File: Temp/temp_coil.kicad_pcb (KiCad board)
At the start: 2 copper layers, 0 parts

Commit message: Updated GUI
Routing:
- net (no net): track 60.0 -> 1086.3 mm

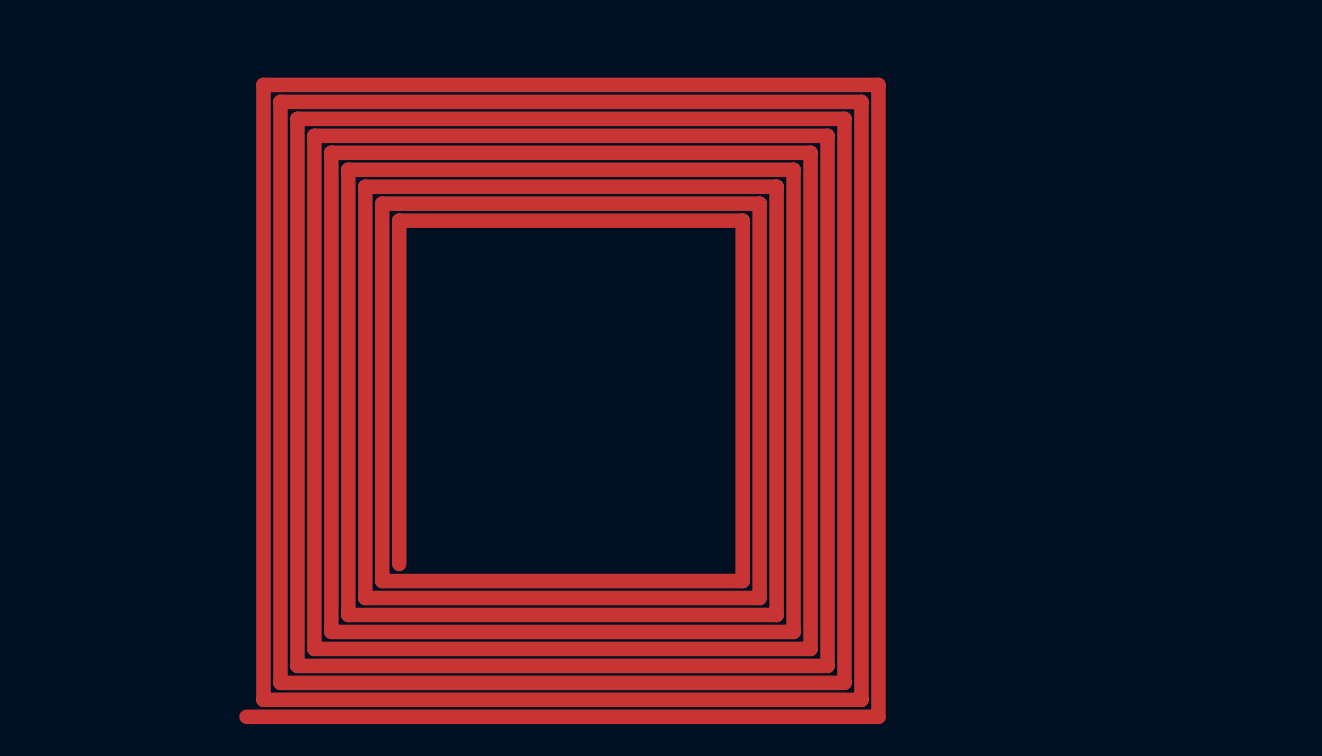
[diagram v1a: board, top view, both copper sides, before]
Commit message: Better Square coil calculation
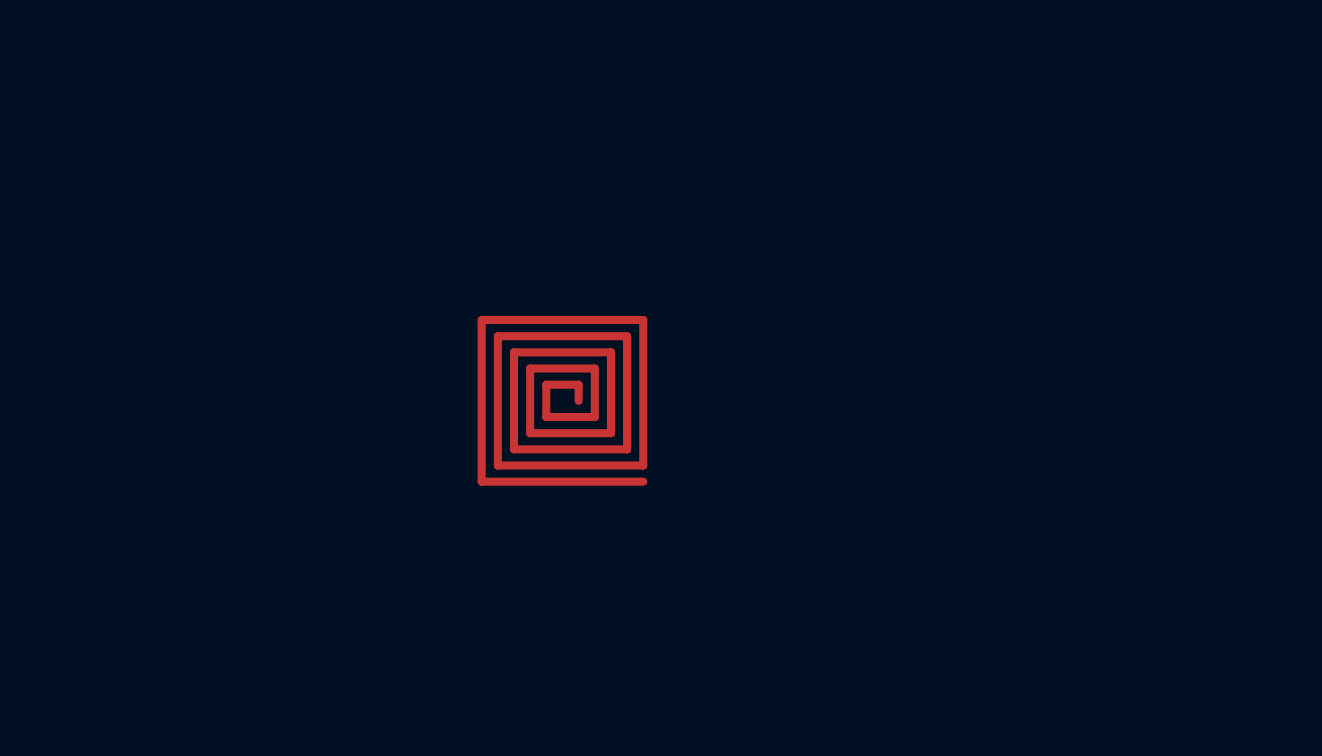
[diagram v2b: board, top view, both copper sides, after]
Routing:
- net (no net): track 1086.3 -> 119.0 mm
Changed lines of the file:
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@@
 	(net 0 "")
 	(segment
-		(start 165.35 84.65)
-		(end 135.7 84.65)
-		(width 0.9)
+		(start 151 99)
+		(end 151 100)
+		(width 0.5)
 		(layer "F.Cu")
 		(net 0)
 	)
 	(segment
-		(start 130.449999 119.55)
-		(end 169.55 119.55)
-		(width 0.9)
+		(start 153 97)
+		(end 153 102)
+		(width 0.5)
 		(layer "F.Cu")
 		(net 0)
 	)
 	(segment
-		(start 131.5 80.45)
-		(end 131.5 118.5)
-		(width 0.9)
+		(start 154 96)
+		(end 154 103)
+		(width 0.5)
 		(layer "F.Cu")
 		(net 0)
 	)
 	(segment
-		(start 162.2 112.2)
-		(end 162.2 87.8)
-		(width 0.9)
+		(start 153 102)
+		(end 148 102)
+		(width 0.5)
 		(layer "F.Cu")
 		(net 0)
 	)
 	(segment
-		(start 136.75 113.25)
-		(end 163.25 113.25)
-		(width 0.9)
+		(start 147 103)
+		(end 147 97)
+		(width 0.5)
 		(layer "F.Cu")
 		(net 0)
 	)
 	(segment
-		(start 138.85 111.15)
-		(end 161.15 111.15)
-		(width 0.9)
+		(start 148 102)
+		(end 148 98)
+		(width 0.5)
 		(layer "F.Cu")
 		(net 0)
 	)
 	(segment
-		(start 137.8 112.2)
-		(end 162.2 112.2)
-		(width 0.9)
+		(start 147 97)
+		(end 153 97)
+		(width 0.5)
 		(layer "F.Cu")
 		(net 0)
 	)
 	(segment
-		(start 168.5 118.5)
-		(end 168.5 81.5)
-		(width 0.9)
+		(start 149 101)
+		(end 149 99)
+		(width 0.5)
 		(layer "F.Cu")
 		(net 0)
 	)
 	(segment
-		(start 163.25 113.25)
-		(end 163.25 86.75)
-		(width 0.9)
+		(start 146 104)
+		(end 146 96)
+		(width 0.5)
 		(layer "F.Cu")
 		(net 0)
 	)
 	(segment
-		(start 165.35 115.35)
-		(end 165.35 84.65)
-		(width 0.9)
+		(start 149 99)
+		(end 151 99)
+		(width 0.5)
 		(layer "F.Cu")
 		(net 0)
 	)
 	(segment
-		(start 164.3 85.7)
-		(end 136.75 85.7)
-		(width 0.9)
+		(start 145 105)
+		(end 145 95)
+		(width 0.5)
 		(layer "F.Cu")
 		(net 0)
 	)
 	(segment
-		(start 166.4 116.4)
-		(end 166.4 83.6)
-		(width 0.9)
+		(start 152 101)
+		(end 149 101)
+		(width 0.5)
 		(layer "F.Cu")
 		(net 0)
 	)
 	(segment
-		(start 137.8 86.75)
-		(end 137.8 112.2)
-		(width 0.9)
+		(start 152 98)
+		(end 152 101)
+		(width 0.5)
 		(layer "F.Cu")
 		(net 0)
 	)
 	(segment
-		(start 132.55 117.45)
-		(end 167.45 117.45)
-		(width 0.9)
+		(start 155 105)
+		(end 145 105)
+		(width 0.5)
 		(layer "F.Cu")
 		(net 0)
 	)
 	(segment
-		(start 167.45 82.55)
-		(end 133.6 82.55)
-		(width 0.9)
+		(start 146 96)
+		(end 154 96)
+		(width 0.5)
 		(layer "F.Cu")
 		(net 0)
 	)
 	(segment
-		(start 135.7 84.65)
-		(end 135.7 114.3)
-		(width 0.9)
+		(start 155 104)
+		(end 146 104)
+		(width 0.5)
 		(layer "F.Cu")
 		(net 0)
 	)
 	(segment
-		(start 161.15 88.85)
-		(end 139.9 88.85)
-		(width 0.9)
+		(start 148 98)
+		(end 152 98)
+		(width 0.5)
 		(layer "F.Cu")
 		(net 0)
 	)
 	(segment
-		(start 163.25 86.75)
-		(end 137.8 86.75)
-		(width 0.9)
+		(start 145 95)
+		(end 155 95)
+		(width 0.5)
 		(layer "F.Cu")
 		(net 0)
 	)
 	(segment
-		(start 135.7 114.3)
-		(end 164.3 114.3)
-		(width 0.9)
+		(start 154 103)
+		(end 147 103)
+		(width 0.5)
 		(layer "F.Cu")
 		(net 0)
 	)
 	(segment
-		(start 136.75 85.7)
-		(end 136.75 113.25)
-		(width 0.9)
+		(start 155 95)
+		(end 155 104)
+		(width 0.5)
 		(layer "F.Cu")
 		(net 0)
-	)
-	(segment
-		(start 134.65 83.6)
-		(end 134.65 115.35)
-		(width 0.9)
-		(layer "F.Cu")
-		(net 0)
-	)
-	(segment
-		(start 133.6 116.4)
-		(end 166.4 116.4)
-		(width 0.9)
-		(layer "F.Cu")
-		(net 0)
-	)
-	(segment
-		(start 167.45 117.45)
-		(end 167.45 82.55)
-		(width 0.9)
-		(layer "F.Cu")
-		(net 0)
-	)
-	(segment
-		(start 133.6 82.55)
-		(end 133.6 116.4)
-		(width 0.9)
-		(layer "F.Cu")
-		(net 0)
-	)
-	(segment
-		(start 134.65 115.35)
-		(end 165.35 115.35)
-		(width 0.9)
-		(layer "F.Cu")
-		(net 0)
-	)
-	(segment
-		(start 132.55 81.5)
-		(end 132.55 117.45)
-		(width 0.9)
-		(layer "F.Cu")
-		(net 0)
-	)
-	(segment
-		(start 164.3 114.3)
-		(end 164.3 85.7)
-		(width 0.9)
-		(layer "F.Cu")
-		(net 0)
-	)
-	(segment
-		(start 138.85 87.8)
-		(end 138.85 111.15)
-		(width 0.9)
-		(layer "F.Cu")
-		(net 0)
-	)
-	(segment
-		(start 169.55 119.55)
-		(end 169.55 80.45)
-		(width 0.9)
-		(layer "F.Cu")
-		(net 0)
-	)
-	(segment
-		(start 168.5 81.5)
-		(end 132.55 81.5)
-		(width 0.9)
-		(layer "F.Cu")
-		(net 0)
-	)
-	(segment
-		(start 169.55 80.45)
-		(end 131.5 80.45)
-		(width 0.9)
-		(layer "F.Cu")
-		(net 0)
-	)
-	(segment
-		(start 139.9 88.85)
-		(end 139.9 110.1)
-		(width 0.9)
-		(layer "F.Cu")
-		(net 0)
-	)
-	(segment
-		(start 161.15 111.15)
-		(end 161.15 88.85)
-		(width 0.9)
-		(layer "F.Cu")
-		(net 0)
-	)
-	(segment
-		(start 162.2 87.8)
-		(end 138.85 87.8)
-		(width 0.9)
-		(layer "F.Cu")
-		(net 0)
-	)
-	(segment
-		(start 131.5 118.5)
-		(end 168.5 118.5)
-		(width 0.9)
-		(layer "F.Cu")
-		(net 0)
-	)
-	(segment
-		(start 166.4 83.6)
-		(end 134.65 83.6)
-		(width 0.9)
-		(layer "F.Cu")
-		(net 0)

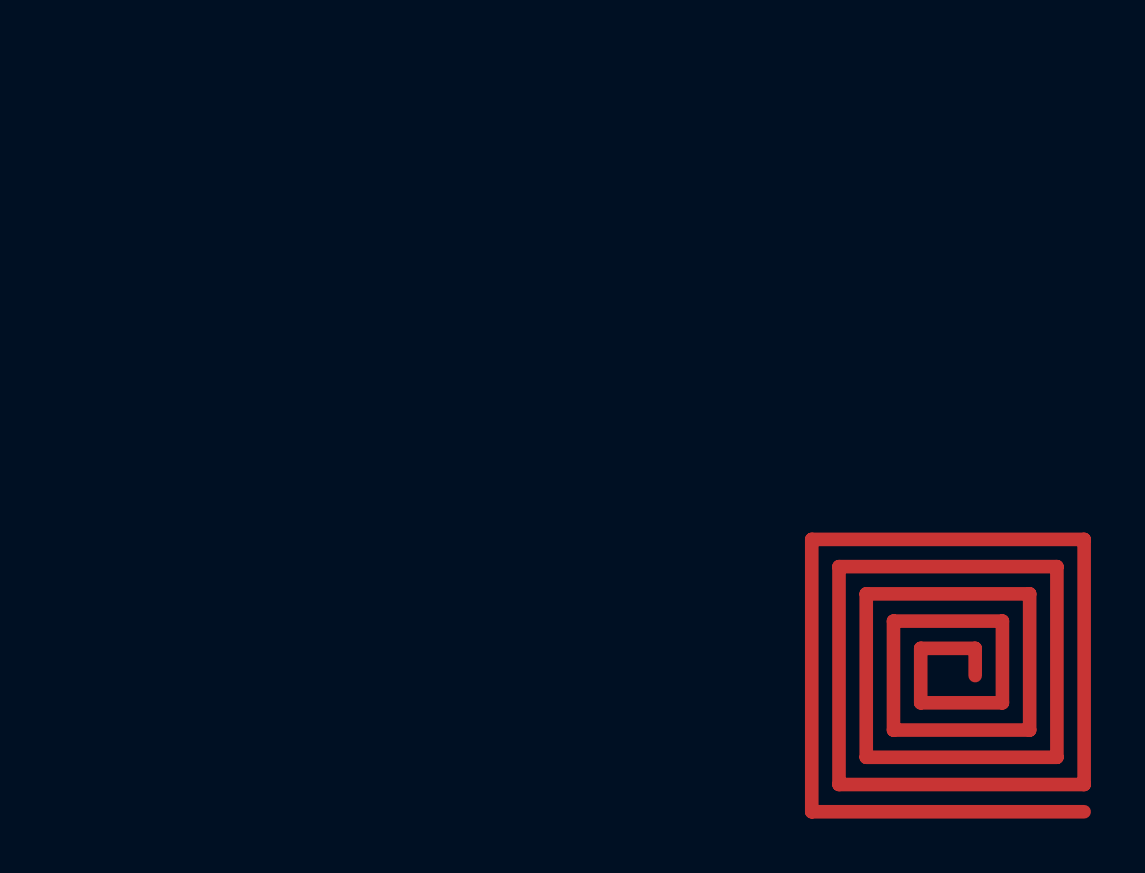
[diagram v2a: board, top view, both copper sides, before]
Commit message: 2 Layer sized (80% of coil) implemented.
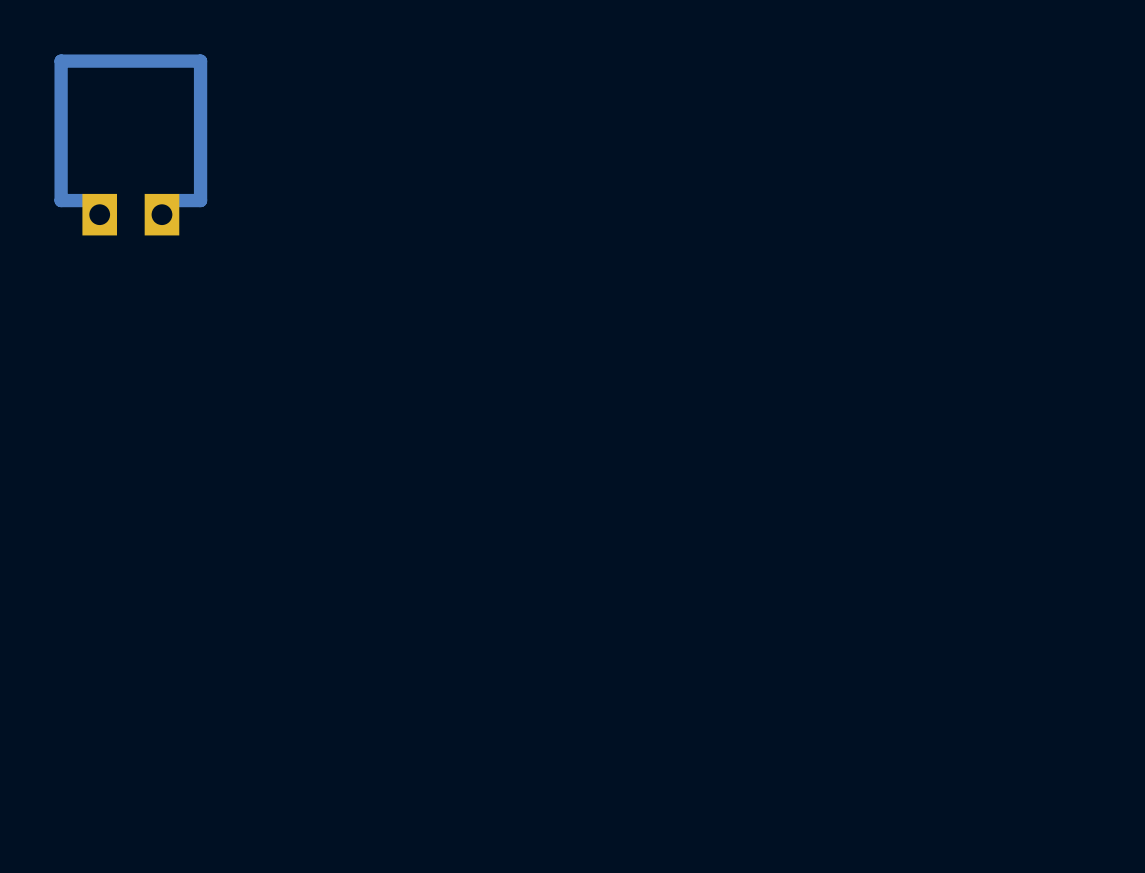
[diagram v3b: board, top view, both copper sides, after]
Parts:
- added ?: , , F.Cu at (0.00, 0.00)
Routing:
- net (no net): track 119.0 -> 16.9 mm
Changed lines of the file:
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@@
 	)
 	(net 0 "")
+	(footprint ""
+		(layer "F.Cu")
+		(at 0 0)
+		(property "Reference" ""
+			(at 0 0 0)
+			(layer "F.SilkS")
+			(effects
+				(font
+					(size 1.27 1.27)
+					(thickness 0.15)
+				)
+			)
+		)
+		(property "Value" ""
+			(at 0 0 0)
+			(layer "F.Fab")
+			(effects
+				(font
+					(size 1.27 1.27)
+					(thickness 0.15)
+				)
+			)
+		)
+		(property "Footprint" ""
+			(at 0 0 0)
+			(layer "F.Fab")
+			(hide yes)
+			(effects
+				(font
+					(size 1.27 1.27)
+					(thickness 0.15)
+				)
+			)
+		)
+		(property "Datasheet" ""
+			(at 0 0 0)
+			(layer "F.Fab")
+			(hide yes)
+			(effects
+				(font
+					(size 1.27 1.27)
+					(thickness 0.15)
+				)
+			)
+		)
+		(property "Description" ""
+			(at 0 0 0)
+			(layer "F.Fab")
+			(hide yes)
+			(effects
+				(font
+					(size 1.27 1.27)
+					(thickness 0.15)
+				)
+			)
+		)
+		(pad "" thru_hole rect
+			(at 118.857 83.07816)
+			(size 1.27 1.524)
+			(drill 0.762)
+			(layers "B.Cu")
+			(remove_unused_layers no)
+			(thermal_bridge_angle 45)
+		)
+		(pad "" thru_hole rect
+			(at 121.143 83.07816)
+			(size 1.27 1.524)
+			(drill 0.762)
+			(layers "B.Cu")
+			(remove_unused_layers no)
+			(thermal_bridge_angle 45)
+		)
+	)
 	(segment
-		(start 151 99)
-		(end 151 100)
-		(width 0.5)
-		(layer "F.Cu")
+		(start 117.44 82.56)
+		(end 117.44 77.44)
+		(width 0.48768)
+		(layer "B.Cu")
 		(net 0)
 	)
 	(segment
-		(start 153 97)
-		(end 153 102)
-		(width 0.5)
-		(layer "F.Cu")
+		(start 117.44 77.44)
+		(end 122.56 77.44)
+		(width 0.48768)
+		(layer "B.Cu")
 		(net 0)
 	)
 	(segment
-		(start 154 96)
-		(end 154 103)
-		(width 0.5)
-		(layer "F.Cu")
+		(start 122.56 82.56)
+		(end 121.778 82.56)
+		(width 0.48768)
+		(layer "B.Cu")
 		(net 0)
 	)
 	(segment
-		(start 153 102)
-		(end 148 102)
-		(width 0.5)
-		(layer "F.Cu")
+		(start 117.44 82.56)
+		(end 118.222 82.56)
+		(width 0.48768)
+		(layer "B.Cu")
 		(net 0)
 	)
 	(segment
-		(start 147 103)
-		(end 147 97)
-		(width 0.5)
-		(layer "F.Cu")
+		(start 122.56 77.44)
+		(end 122.56 82.56)
+		(width 0.48768)
+		(layer "B.Cu")
 		(net 0)
 	)
-	(segment
-		(start 148 102)
-		(end 148 98)
-		(width 0.5)
-		(layer "F.Cu")
-		(net 0)
-	)
-	(segment
-		(start 147 97)
-		(end 153 97)
-		(width 0.5)
-		(layer "F.Cu")
-		(net 0)
-	)
-	(segment
-		(start 149 101)
-		(end 149 99)
-		(width 0.5)
-		(layer "F.Cu")
-		(net 0)
-	)
-	(segment
-		(start 146 104)
-		(end 146 96)
-		(width 0.5)
-		(layer "F.Cu")
-		(net 0)
-	)
-	(segment
-		(start 149 99)
-		(end 151 99)
-		(width 0.5)
-		(layer "F.Cu")
-		(net 0)
-	)
-	(segment
-		(start 145 105)
-		(end 145 95)
-		(width 0.5)
-		(layer "F.Cu")
-		(net 0)
-	)
-	(segment
-		(start 152 101)
-		(end 149 101)
-		(width 0.5)
-		(layer "F.Cu")
-		(net 0)
-	)
-	(segment
-		(start 152 98)
-		(end 152 101)
-		(width 0.5)
-		(layer "F.Cu")
-		(net 0)
-	)
-	(segment
-		(start 155 105)
-		(end 145 105)
-		(width 0.5)
-		(layer "F.Cu")
-		(net 0)
-	)
-	(segment
-		(start 146 96)
-		(end 154 96)
-		(width 0.5)
-		(layer "F.Cu")
-		(net 0)
-	)
-	(segment
-		(start 155 104)
-		(end 146 104)
-		(width 0.5)
-		(layer "F.Cu")
-		(net 0)
-	)
-	(segment
-		(start 148 98)
-		(end 152 98)
-		(width 0.5)
-		(layer "F.Cu")
-		(net 0)
-	)
-	(segment
-		(start 145 95)
-		(end 155 95)
-		(width 0.5)
-		(layer "F.Cu")
-		(net 0)
-	)
-	(segment
-		(start 154 103)
-		(end 147 103)
-		(width 0.5)
-		(layer "F.Cu")
-		(net 0)
-	)
-	(segment
-		(start 155 95)
-		(end 155 104)
-		(width 0.5)
-		(layer "F.Cu")
-		(net 0)
-	)
